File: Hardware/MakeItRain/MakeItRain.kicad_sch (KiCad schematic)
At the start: 15 parts, among them J1 Conn_02x14_Odd_Even, J2 Conn_02x19_Odd_Even, J3 Conn_01x19, U1 MCP23008-xP

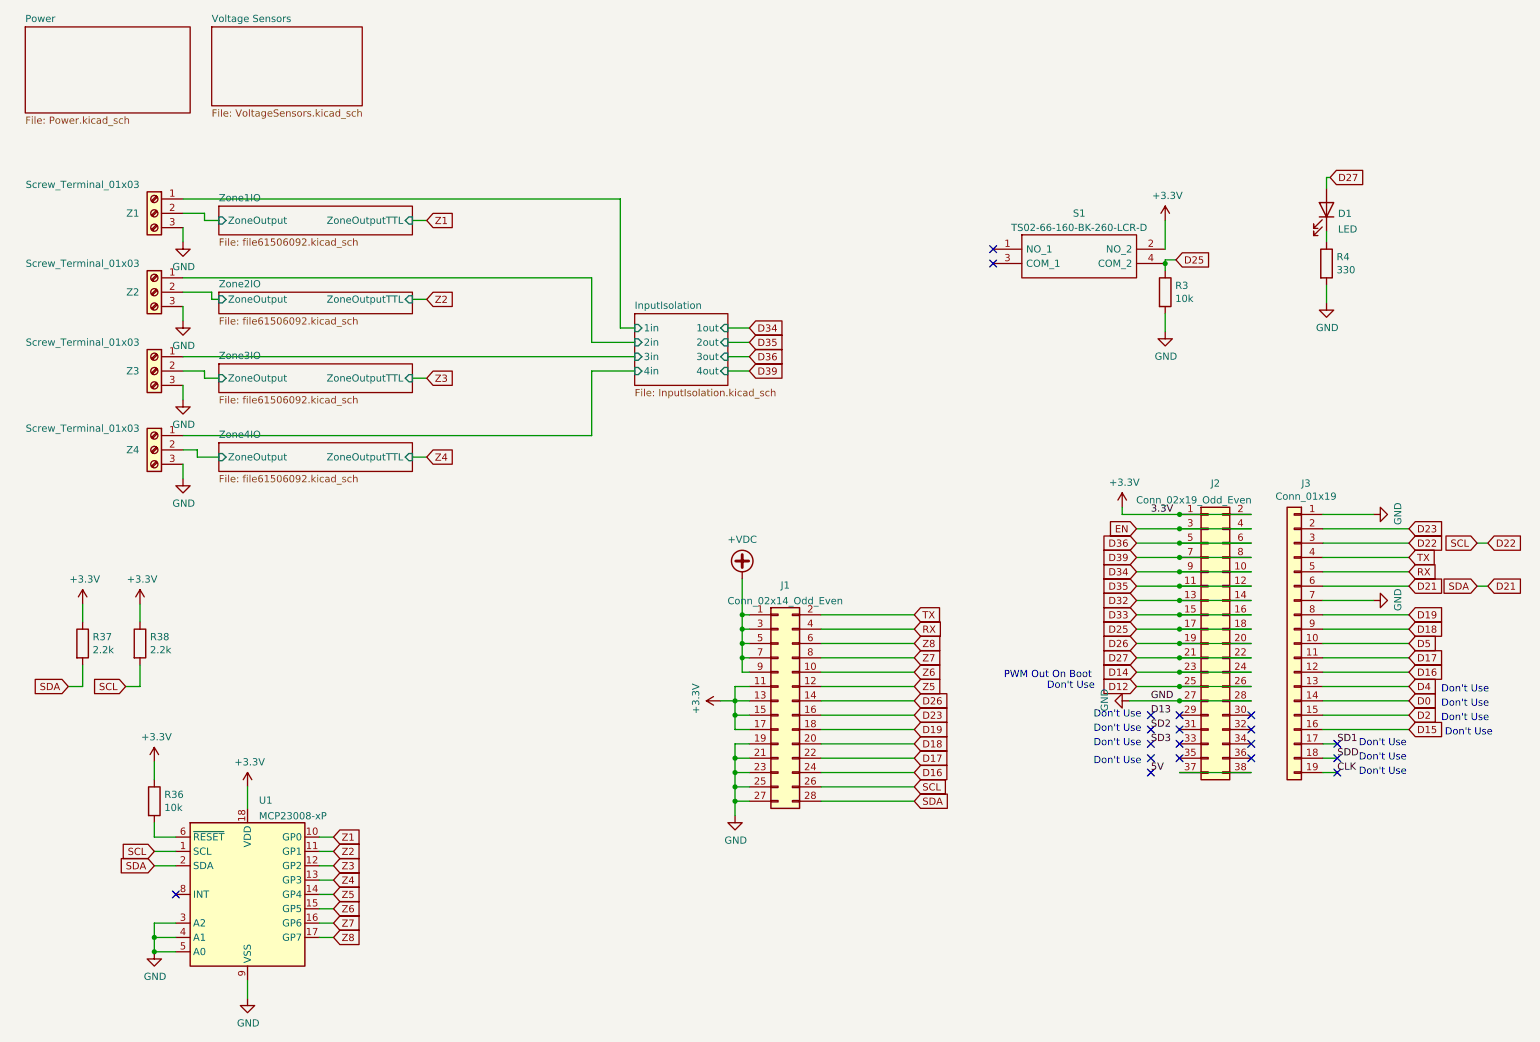
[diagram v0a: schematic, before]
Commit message: wip for adding RTC
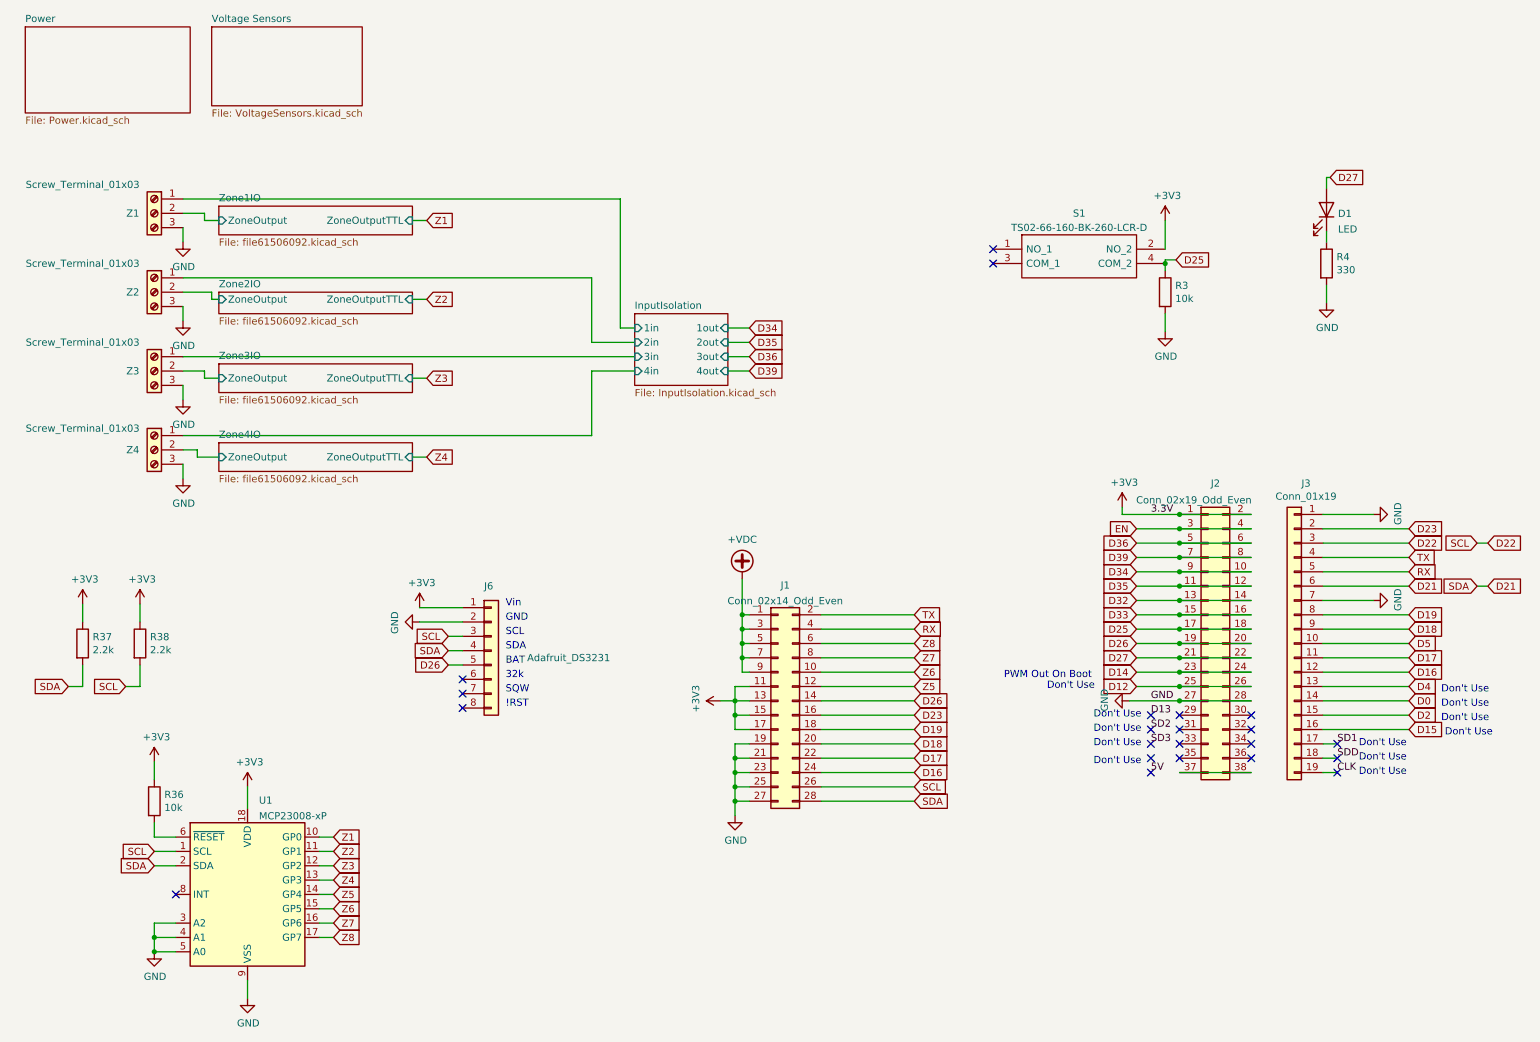
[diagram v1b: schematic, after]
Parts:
- added J6: Adafruit_DS3231, Connector_PinHeader_1.00mm:PinHeader_1x08_P1.00mm_Vertical_SMD_Pin1Right, symbol Connector_Generic:Conn_01x08
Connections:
- net +3V3: now also J6.1 (Pin_1)
- net D21: now also J6.4 (Pin_4)
- net D22: now also J6.3 (Pin_3)
- net D26: now also J6.5 (Pin_5)
- net GND: now also J6.2 (Pin_2)
- no-connect marks 19 -> 22
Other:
- note added: "!RST"
- note added: "32k"
- note added: "BAT"
- note added: "GND"
- note added: "SCL"
- note added: "SDA"
- note added: "SQW"
- note added: "Vin"

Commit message: wip
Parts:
- removed J6: Adafruit_DS3231, Connector_PinHeader_1.00mm:PinHeader_1x08_P1.00mm_Vertical_SMD_Pin1Right, symbol Connector_Generic:Conn_01x08
- added C5: 0.1uF, Capacitor_THT:C_Rect_L9.0mm_W3.6mm_P7.50mm_MKT, symbol Device:C
- added IC3: DS3231SN#, SamacSys_Parts:SOIC127P1032X265-16N, symbol SamacSys_Parts:DS3231SN#
- added U3: S8411-45R, SamacSys_Parts:S8411-45R_1, symbol SamacSys_Parts:S8411-45R
- R3, R36, R37, R38, R4: footprint Resistor_THT:R_Axial_DIN0207_L6.3mm_D2.5mm_P2.54mm_Vertical -> Resistor_SMD:R_1206_3216Metric_Pad1.30x1.75mm_HandSolder
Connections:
- net +3V3: now also C5.1, IC3.2 (VCC)
- net D21: now also IC3.15 (SDA)
- net D22: now also IC3.16 (SCL)
- net D26: now also IC3.14 (VBAT), U3.1 (+)
- net GND: now also C5.2, IC3.10 (N.C._6), IC3.11 (N.C._7), IC3.12 (N.C._8), IC3.13 (GND), IC3.5 (N.C._1), IC3.6 (N.C._2), IC3.7 (N.C._3), IC3.8 (N.C._4), IC3.9 (N.C._5), U3.2 (-)
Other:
- note removed: "!RST"
- note removed: "32k"
- note removed: "BAT"
- note removed: "GND"
- note removed: "SCL"
- note removed: "SDA"
- note removed: "SQW"
- note removed: "Vin"
